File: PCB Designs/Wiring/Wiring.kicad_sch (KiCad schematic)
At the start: 11 parts, among them M1 TL Servo, M2 BL Servo, M3 TR Servo, M4 BR Servo, M5 Left Motor, M6 Right Motor, U2 L298N, U5 ESP32-C3-DevKitM-1

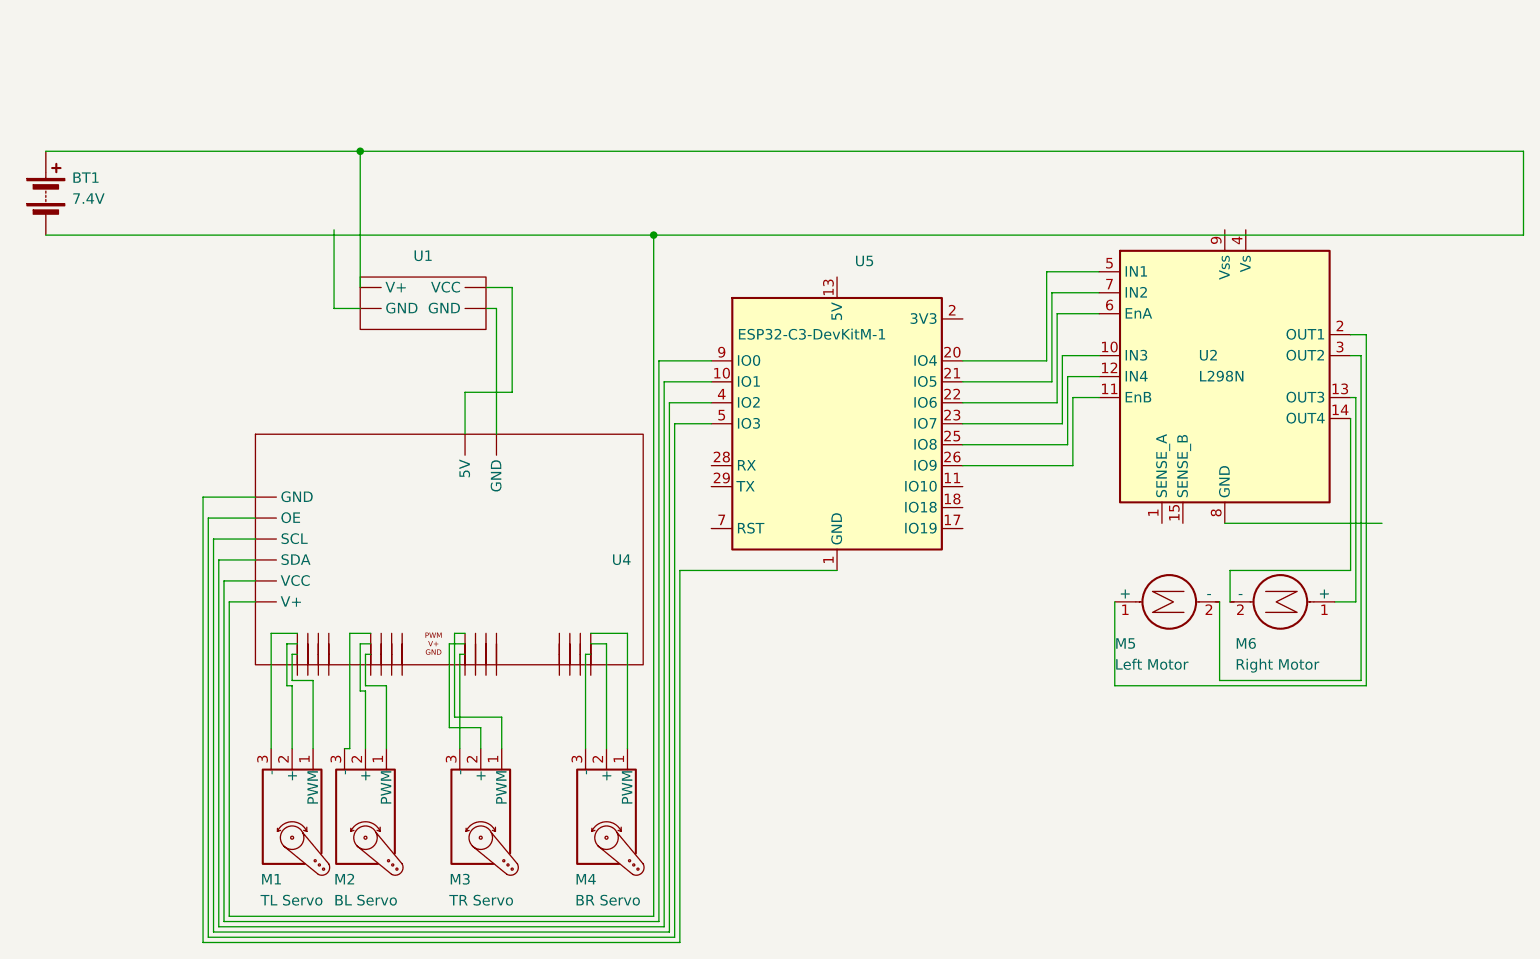
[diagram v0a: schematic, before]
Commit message: Added MPU 6050 to wiring
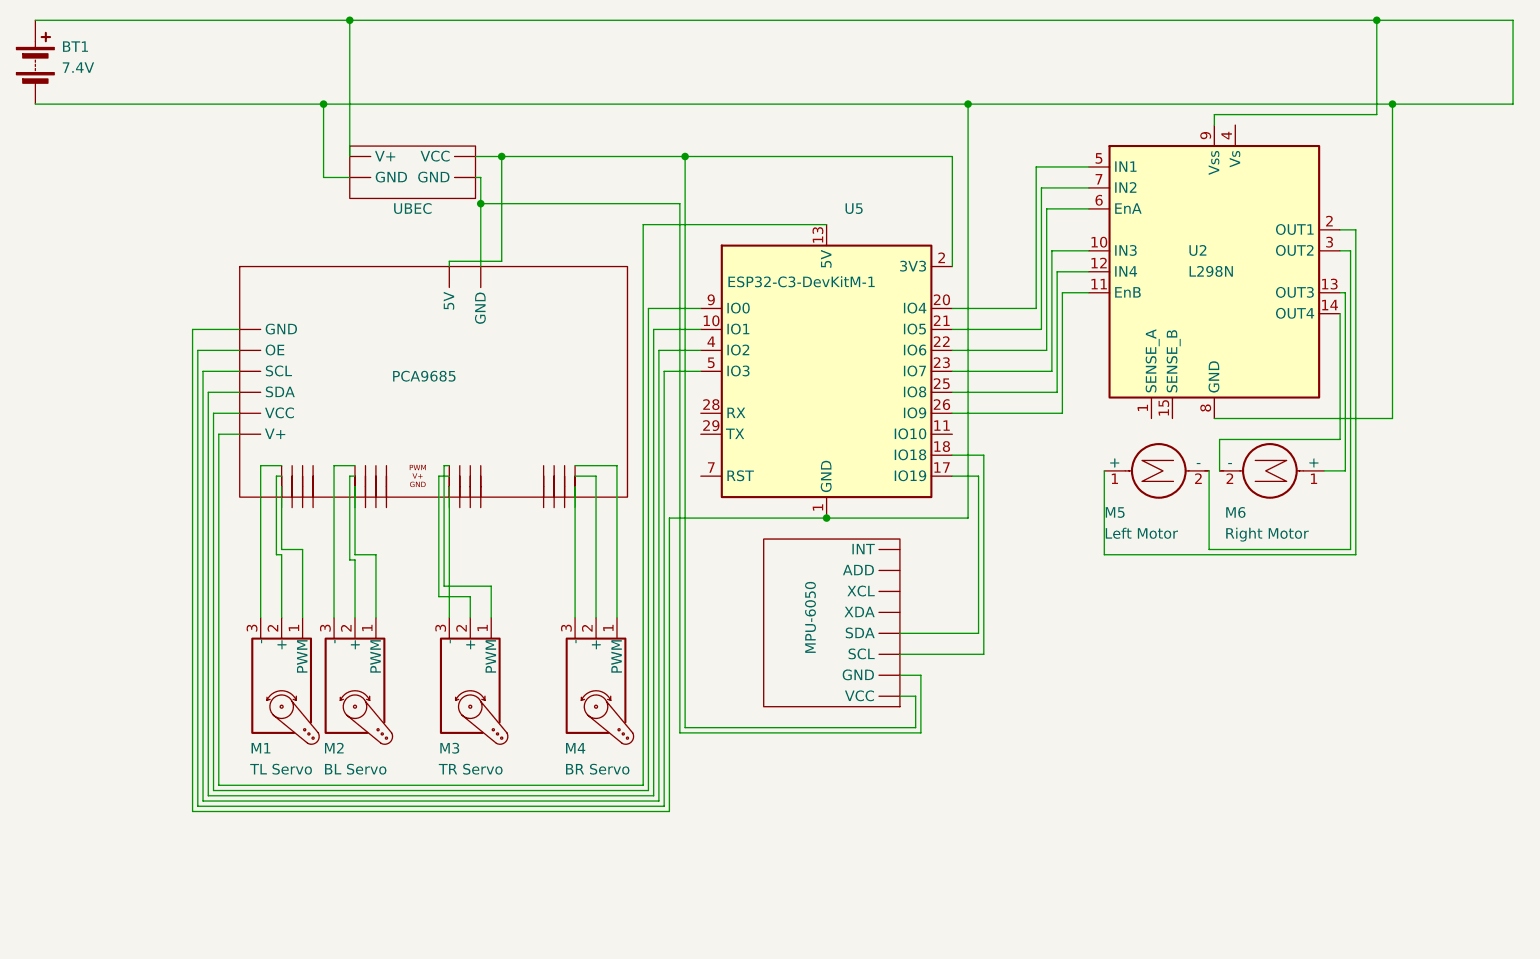
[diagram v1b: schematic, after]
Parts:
- added MPU-6050: (no value), symbol Custom Breakout Boards:MPU6050
- renumbered U4 to PCA9685, U1 to UBEC
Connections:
- net at PCA9685., U5.1 (GND), U5.12 (GND)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: now also BT1.1 (+), BT1.2 (-), U2.8 (GND), U2.9 (Vss), UBEC. (GND)
- net at U5.13 (5V), U5.14 (5V): now also PCA9685.
- net at U5.17 (IO19): now also MPU-6050. (INT)
- net at U5.18 (IO18): now also MPU-6050. (INT)
- net at U5.2 (3V3), U5.3 (3V3): now also PCA9685., UBEC. (GND), MPU-6050. (INT)
- net at PCA9685.: now also M1.3 (-)
- new net: MPU-6050. (INT), PCA9685., UBEC. (GND)
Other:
- moved on the sheet: BT1, M1, M2, M3, M4, M5, M6, PCA9685, U2, U5, UBEC
